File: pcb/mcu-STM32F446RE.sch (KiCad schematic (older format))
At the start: 24 parts

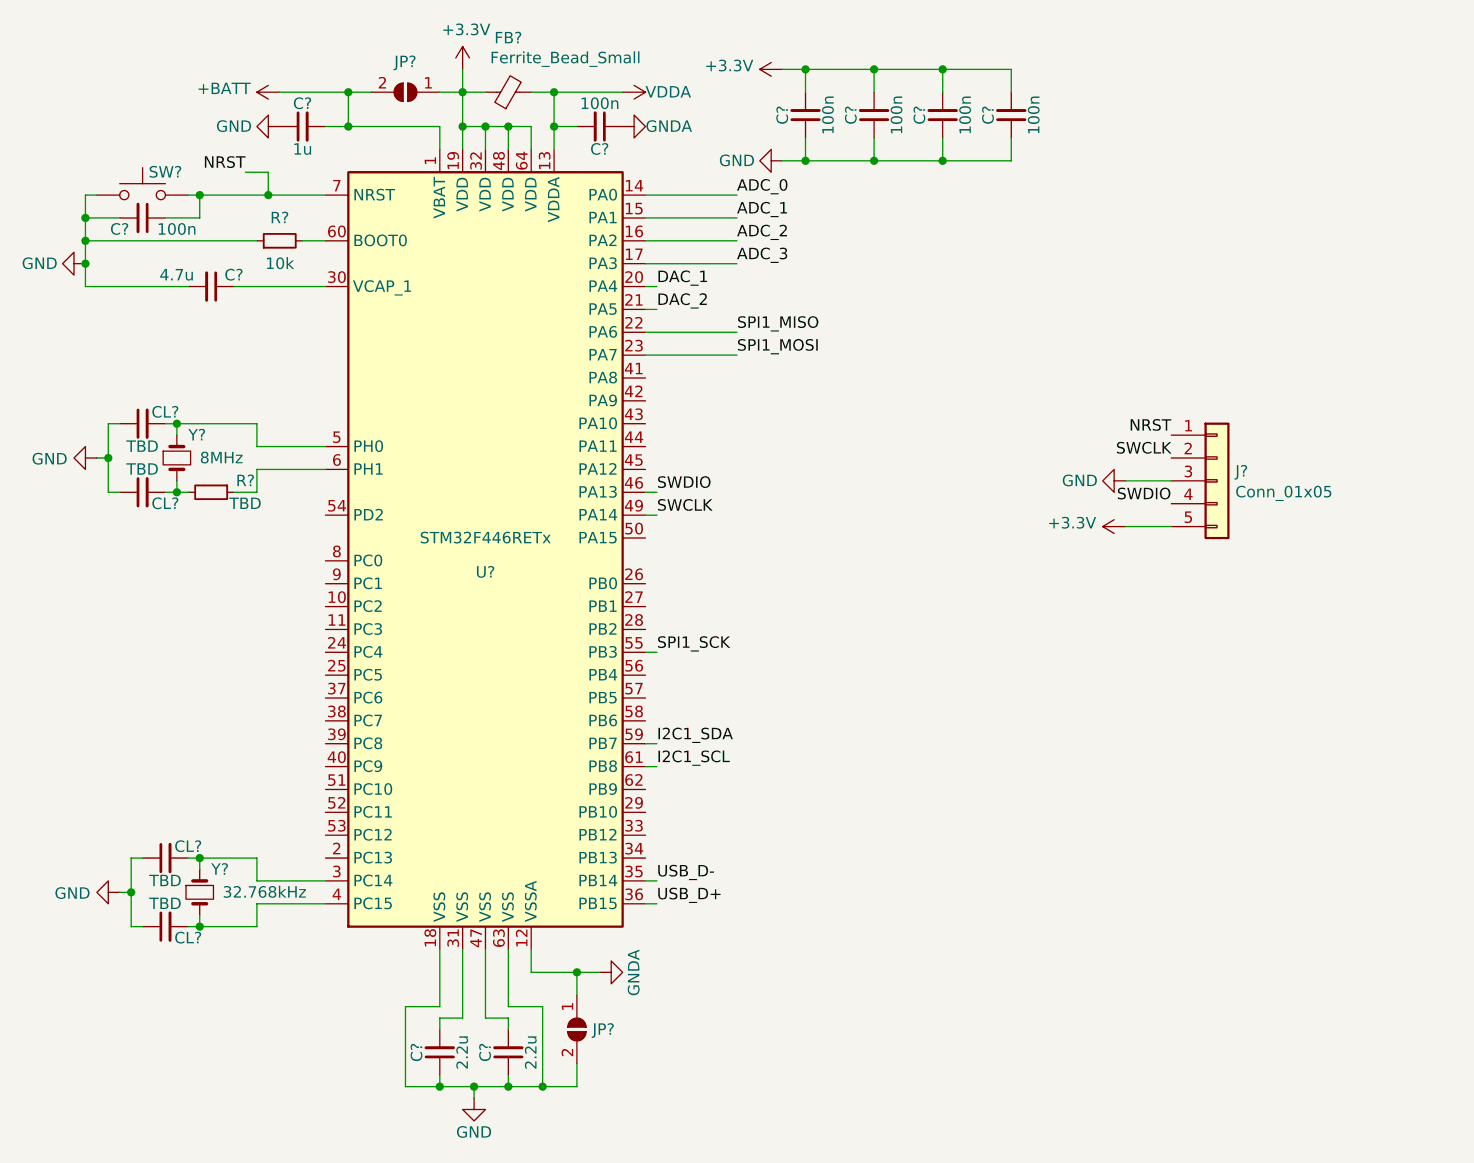
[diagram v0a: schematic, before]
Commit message: [PCB] update mcu config & pwr converter, add sd card
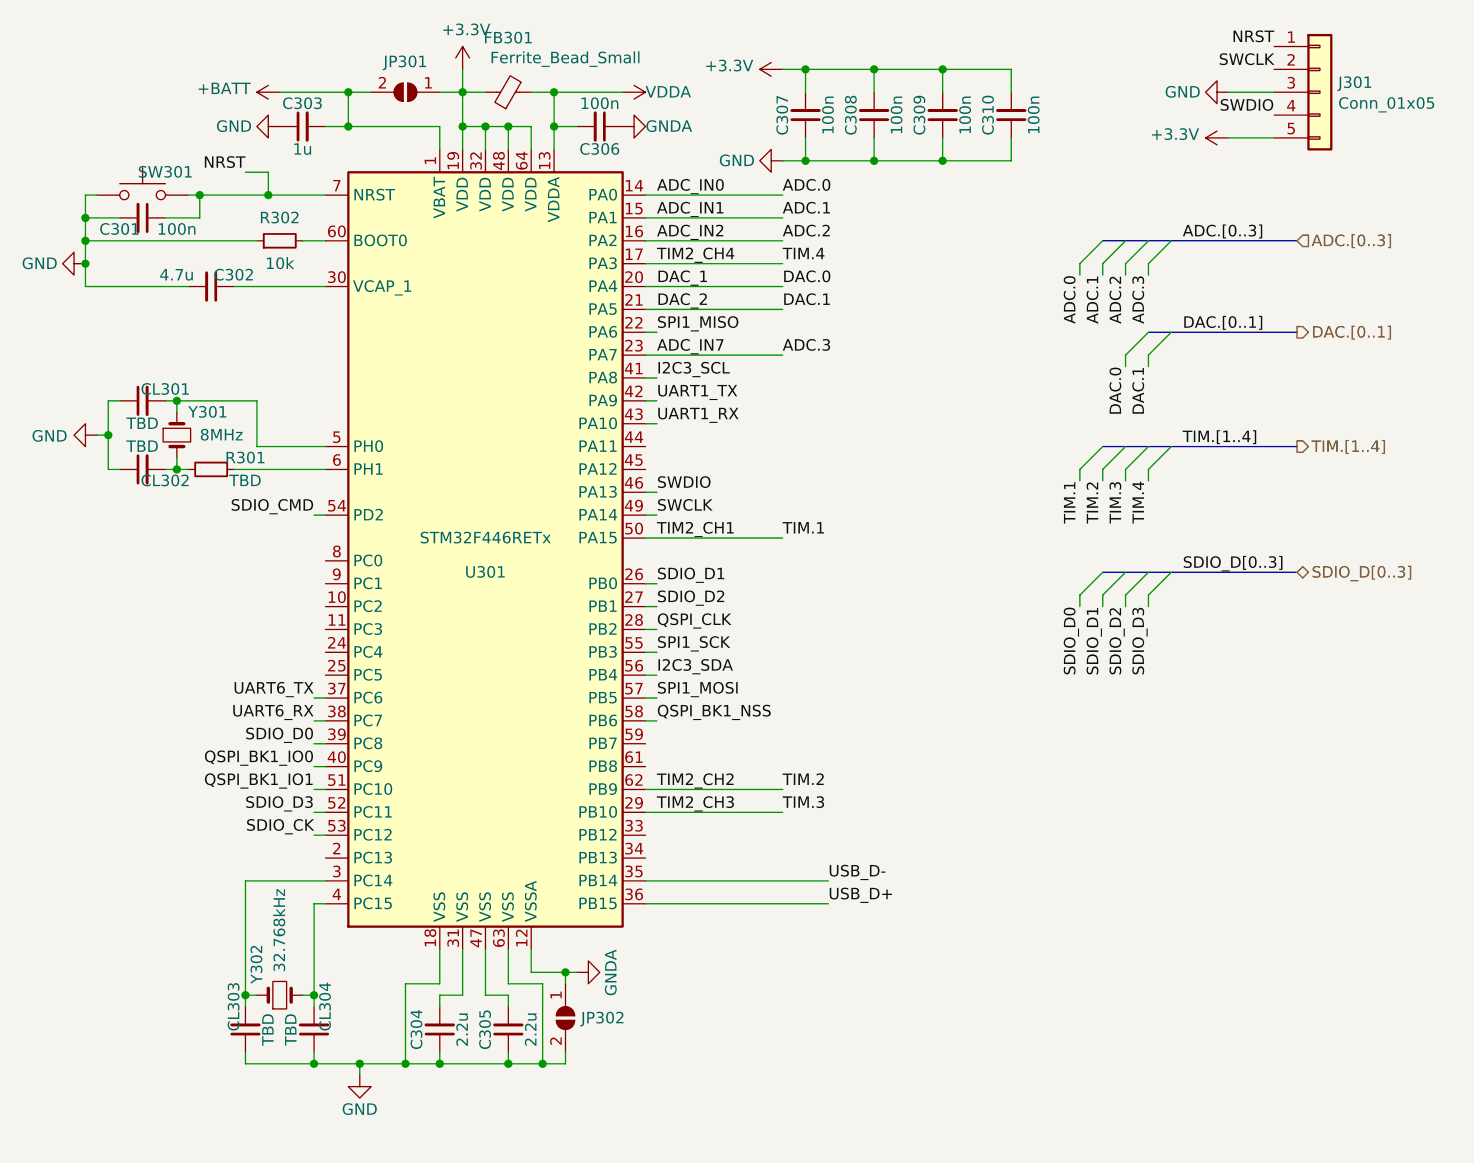
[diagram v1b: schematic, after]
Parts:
- gave numbers to parts that had none: 24
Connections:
- net SPI1_MOSI: now also U301.57 (PB5); no longer U301.23 (PA7)
- net SDIO_D1: now reaches U301.26 (PB0)
- net SDIO_D2: now reaches U301.27 (PB1)
- net QSPI_CLK: now reaches U301.28 (PB2)
- net TIM.3: now reaches U301.29 (PB10)
- net UART6_TX: now reaches U301.37 (PC6)
- net UART6_RX: now reaches U301.38 (PC7)
- net SDIO_D0: now reaches U301.39 (PC8)
- net QSPI_BK1_IO0: now reaches U301.40 (PC9)
- net I2C3_SCL: now reaches U301.41 (PA8)
- net UART1_TX: now reaches U301.42 (PA9)
- net UART1_RX: now reaches U301.43 (PA10)
- net TIM.1: now reaches U301.50 (PA15)
- net QSPI_BK1_IO1: now reaches U301.51 (PC10)
- net SDIO_D3: now reaches U301.52 (PC11)
- net SDIO_CK: now reaches U301.53 (PC12)
- net SDIO_CMD: now reaches U301.54 (PD2)
- net I2C3_SDA: now reaches U301.56 (PB4)
- net QSPI_BK1_NSS: now reaches U301.58 (PB6)
- net TIM.2: now reaches U301.62 (PB9)
- net ADC_0 renamed ADC.0
- net ADC_1 renamed ADC.1
- net ADC_2 renamed ADC.2
- net ADC_3 renamed TIM.4
- net DAC_1 renamed DAC.0
- net DAC_2 renamed DAC.1
- net I2C1_SCL: no longer names the net of U301.61 (PB8)
- net I2C1_SDA: no longer names the net of U301.59 (PB7)
- new net ADC.3: U301.23 (PA7)
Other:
- moved on the sheet: C304, C305, CL301, CL302, CL303, CL304, J301, JP302, R301, Y301, Y302

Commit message: [PCB] minor changes
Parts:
- removed C301, C306, C307, C308, C309, C310: 100n, symbol Device:C_Small
- removed C302: 4.7u, symbol Device:C_Small
- removed C303: 1u, symbol Device:C_Small
- removed C304, C305: 2.2u, symbol Device:C_Small
- removed CL301, CL302, CL303, CL304: TBD, symbol Device:C_Small
- removed R301: TBD, symbol Device:R_Small
- removed Y302: 32.768kHz, symbol Device:Crystal_Small
- added C? (x4): TBD, Capacitor_SMD:C_0603_1608Metric, symbol Device:C_Small
- added C? (x2): 2.2u, Capacitor_SMD:C_0603_1608Metric, symbol Device:C_Small
- added C? (x6): 100n, Capacitor_SMD:C_0603_1608Metric, symbol Device:C_Small
- added C?: 4.7u, Capacitor_SMD:C_0603_1608Metric, symbol Device:C_Small
- added C?: 1u, Capacitor_SMD:C_0603_1608Metric, symbol Device:C_Small
- added R?: TBD, symbol Device:R_Small
- added Y?: 32.768kHz, symbol Device:Crystal_Small
- FB301: footprint (none) -> Capacitor_SMD:C_0603_1608Metric
- J301: footprint (none) -> Connector_PinHeader_2.54mm:PinHeader_1x05_P2.54mm_Horizontal
- JP301, JP302: footprint (none) -> Jumper:SolderJumper-2_P1.3mm_Open_TrianglePad1.0x1.5mm
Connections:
- net QSPI_BK1_NSS is gone; now on net UART1_TX: U301.58 (PB6)
- net +3V3: no longer FB301.1, JP301.1 (A), U301.19 (VDD), U301.32 (VDD), U301.48 (VDD), U301.64 (VDD)
- net +BATT: now also JP301.1 (A), C?.1; no longer JP301.2 (B)
- net GND: now also JP302.1 (A), C?.2, C?.2, C?.2, C?.2, C?.2, C?.2, C?.2, C?.2, C?.2, C?.2, C?.2, C?.2, C?.2; no longer JP302.2 (B)
- net GNDA: now also JP302.2 (B), C?.1; no longer JP302.1 (A)
- net NRST: now also C?.1
- net TIM.1: now also U301.61 (PB8); no longer U301.50 (PA15)
- net UART1_TX: no longer U301.42 (PA9)
- net VDDA: now also C?.2
- net SPI_SO: now reaches U301.10 (PC2)
- net at U301.3 (PC14): now also C?.1, Y?.1
- net at U301.30 (VCAP_1): now also C?.1
- net at U301.31 (VSS): now also C?.1
- net SPI_NSS: now reaches U301.33 (PB12)
- net SPI_SCLK: now reaches U301.34 (PB13)
- net at U301.4 (PC15): now also C?.1, Y?.2
- net at U301.47 (VSS): now also C?.1
- net at U301.5 (PH0), Y301.1: now also C?.1
- net at U301.6 (PH1): now also R?.2
- net SPI_SI: now reaches U301.9 (PC1)
- net at Y301.2: now also C?.1, R?.1
- net I2C3_SCL renamed I2C_SCL
- net I2C3_SDA renamed I2C_SDA
- net QSPI_BK1_IO0: no longer names the net of U301.40 (PC9)
- net QSPI_BK1_IO1: no longer names the net of U301.51 (PC10)
- net UART6_RX renamed UART2_RX
- net UART6_TX renamed UART2_TX
- new net 3.3V: C?.1, C?.1, C?.1, C?.1, FB301.1, JP301.2 (B), U301.19 (VDD), U301.32 (VDD), U301.48 (VDD), U301.64 (VDD)
- new net I2C_SMBA: U301.42 (PA9)
- new net SPI1_NSS: U301.50 (PA15)
